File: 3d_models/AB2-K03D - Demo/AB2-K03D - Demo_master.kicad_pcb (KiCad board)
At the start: 2 copper layers, 209 parts

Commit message: AB2-K03D: rename master file
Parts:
- added AB2_STANDOFF_1.96x1.96_BOARD_ROUNDED_CORNERS_KEEPOUT_FR4: VAL**, AB2_STANDOFF_1.96x1.96_BOARD_ROUNDED_CORNERS_KEEPOUT_FR4, F.Cu at (304.8, 166.4)
- added AB2_STANDOFF_1.96x3.92_BOARD_ROUNDED_CORNERS_KEEPOUT_FR4: VAL**, AB2_STANDOFF_1.96x3.92_BOARD_ROUNDED_CORNERS_KEEPOUT_FR4, F.Cu at (356.9, 166.4)
- added AB2_STANDOFF_3.92x3.92_BOARD_ROUNDED_CORNERS_KEEPOUT_FR4: VAL**, AB2_STANDOFF_3.92x3.92_BOARD_ROUNDED_CORNERS_KEEPOUT_FR4, F.Cu at (306.1, 268.0)
- added ROT_ENC1: AB2_ROT_ENC_W_SW, AB2_ROTARY_ENCODER_W_SWITCH, F.Cu at (20.3, 196.8)

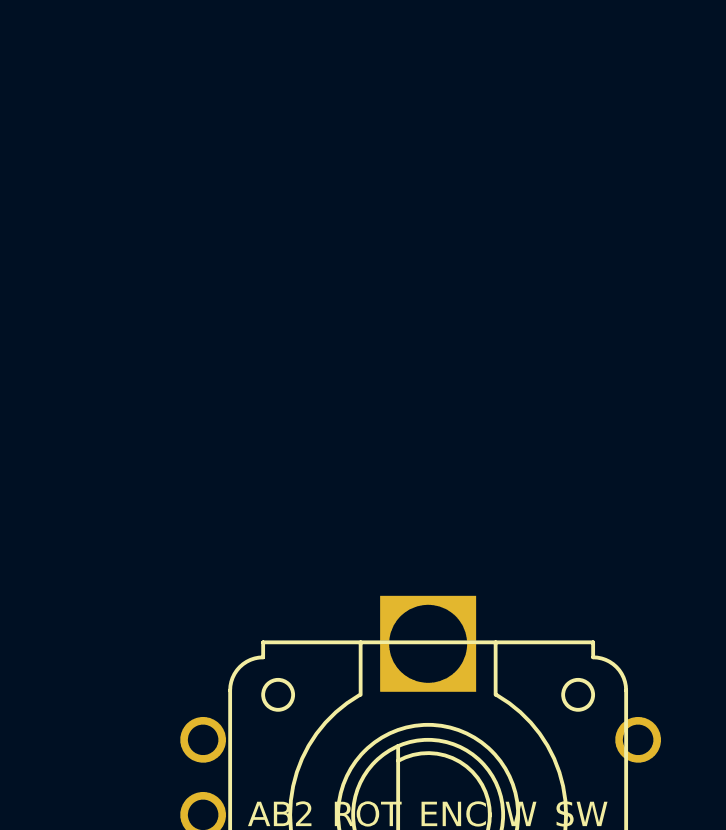
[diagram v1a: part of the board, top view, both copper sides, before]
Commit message: AB2-K03D: add 0805 LED RED/YEL/GRN/BLU
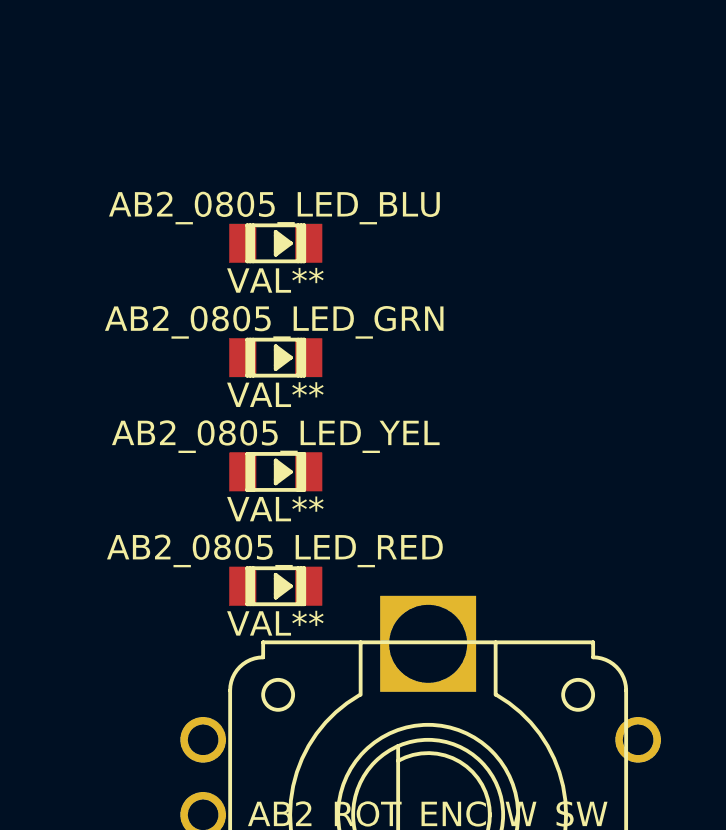
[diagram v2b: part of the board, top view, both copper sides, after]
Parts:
- added AB2_0805_LED_BLU: VAL**, AB2_0805_LED_BLU, F.Cu at (15.2, 177.8)
- added AB2_0805_LED_GRN: VAL**, AB2_0805_LED_GRN, F.Cu at (15.2, 181.6)
- added AB2_0805_LED_RED: VAL**, AB2_0805_LED_RED, F.Cu at (15.2, 189.2)
- added AB2_0805_LED_YEL: VAL**, AB2_0805_LED_YEL, F.Cu at (15.2, 185.4)
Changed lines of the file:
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@@
     (tracks 0)
     (zones 0)
-    (modules 213)
+    (modules 217)
     (nets 9)
   )
@@
     )
   )
+  (module AB2_0805_LED_RED (layer F.Cu)
+    (at 15.24 189.23)
+    (fp_text reference AB2_0805_LED_RED (at 0 -1.27) (layer F.SilkS)
+      (effects (font (size 0.8128 0.8128) (thickness 0.0762)))
+    )
+    (fp_text value VAL** (at 0 1.27) (layer F.SilkS)
+      (effects (font (size 0.8128 0.8128) (thickness 0.0762)))
+    )
+    (fp_line (start 0.254 -0.127) (end 0.254 0.127) (layer F.SilkS) (width 0.127))
+    (fp_line (start 0.381 0) (end 0 0.254) (layer F.SilkS) (width 0.127))
+    (fp_line (start 0.381 0) (end 0 -0.254) (layer F.SilkS) (width 0.127))
+    (fp_line (start 0.127 -0.254) (end 0.127 0.254) (layer F.SilkS) (width 0.127))
+    (fp_line (start 0 -0.381) (end 0 0.381) (layer F.SilkS) (width 0.127))
+    (fp_line (start 0 0.381) (end 0.508 0) (layer F.SilkS) (width 0.127))
+    (fp_line (start 0.508 0) (end 0 -0.381) (layer F.SilkS) (width 0.127))
+    (fp_line (start 0.85 0.6) (end 0.85 -0.6) (layer F.SilkS) (width 0.127))
+    (fp_line (start 0.75 -0.6) (end 0.75 0.6) (layer F.SilkS) (width 0.127))
+    (fp_line (start -0.85 0.6) (end -0.85 -0.6) (layer F.SilkS) (width 0.127))
+    (fp_line (start -0.75 -0.6) (end -0.75 0.6) (layer F.SilkS) (width 0.127))
+    (fp_line (start -0.95 -0.6) (end 0.95 -0.6) (layer F.SilkS) (width 0.127))
+    (fp_line (start 0.95 -0.6) (end 0.95 0.6) (layer F.SilkS) (width 0.127))
+    (fp_line (start 0.95 0.6) (end -0.95 0.6) (layer F.SilkS) (width 0.127))
+    (fp_line (start -0.95 0.6) (end -0.95 -0.6) (layer F.SilkS) (width 0.127))
+    (pad 1 smd rect (at -1.1 0) (size 0.9 1.3)
+      (layers F.Cu F.Paste F.Mask)
+    )
+    (pad 2 smd rect (at 1.1 0) (size 0.9 1.3)
+      (layers F.Cu F.Paste F.Mask)
+    )
+    (model ../3d_models/ab2_passive/AB2_0805_LED_RED.wrl
+      (at (xyz 0 0 0))
+      (scale (xyz 0.3937 0.3937 0.3937))
+      (rotate (xyz 0 0 0))
+    )
+  )
+  (module AB2_0805_LED_YEL (layer F.Cu)
+    (at 15.24 185.42)
+    (fp_text reference AB2_0805_LED_YEL (at 0 -1.27) (layer F.SilkS)
+      (effects (font (size 0.8128 0.8128) (thickness 0.0762)))
+    )
+    (fp_text value VAL** (at 0 1.27) (layer F.SilkS)
+      (effects (font (size 0.8128 0.8128) (thickness 0.0762)))
+    )
+    (fp_line (start 0.254 -0.127) (end 0.254 0.127) (layer F.SilkS) (width 0.127))
+    (fp_line (start 0.381 0) (end 0 0.254) (layer F.SilkS) (width 0.127))
+    (fp_line (start 0.381 0) (end 0 -0.254) (layer F.SilkS) (width 0.127))
+    (fp_line (start 0.127 -0.254) (end 0.127 0.254) (layer F.SilkS) (width 0.127))
+    (fp_line (start 0 -0.381) (end 0 0.381) (layer F.SilkS) (width 0.127))
+    (fp_line (start 0 0.381) (end 0.508 0) (layer F.SilkS) (width 0.127))
+    (fp_line (start 0.508 0) (end 0 -0.381) (layer F.SilkS) (width 0.127))
+    (fp_line (start 0.85 0.6) (end 0.85 -0.6) (layer F.SilkS) (width 0.127))
+    (fp_line (start 0.75 -0.6) (end 0.75 0.6) (layer F.SilkS) (width 0.127))
+    (fp_line (start -0.85 0.6) (end -0.85 -0.6) (layer F.SilkS) (width 0.127))
+    (fp_line (start -0.75 -0.6) (end -0.75 0.6) (layer F.SilkS) (width 0.127))
+    (fp_line (start -0.95 -0.6) (end 0.95 -0.6) (layer F.SilkS) (width 0.127))
+    (fp_line (start 0.95 -0.6) (end 0.95 0.6) (layer F.SilkS) (width 0.127))
+    (fp_line (start 0.95 0.6) (end -0.95 0.6) (layer F.SilkS) (width 0.127))
+    (fp_line (start -0.95 0.6) (end -0.95 -0.6) (layer F.SilkS) (width 0.127))
+    (pad 1 smd rect (at -1.1 0) (size 0.9 1.3)
+      (layers F.Cu F.Paste F.Mask)
+    )
+    (pad 2 smd rect (at 1.1 0) (size 0.9 1.3)
+      (layers F.Cu F.Paste F.Mask)
+    )
+    (model ../3d_models/ab2_passive/AB2_0805_LED_YEL.wrl
+      (at (xyz 0 0 0))
+      (scale (xyz 0.3937 0.3937 0.3937))
+      (rotate (xyz 0 0 0))
+    )
+  )
+  (module AB2_0805_LED_GRN (layer F.Cu)
+    (at 15.24 181.61)
+    (fp_text reference AB2_0805_LED_GRN (at 0 -1.27) (layer F.SilkS)
+      (effects (font (size 0.8128 0.8128) (thickness 0.0762)))
+    )
+    (fp_text value VAL** (at 0 1.27) (layer F.SilkS)
+      (effects (font (size 0.8128 0.8128) (thickness 0.0762)))
+    )
+    (fp_line (start 0.254 -0.127) (end 0.254 0.127) (layer F.SilkS) (width 0.127))
+    (fp_line (start 0.381 0) (end 0 0.254) (layer F.SilkS) (width 0.127))
+    (fp_line (start 0.381 0) (end 0 -0.254) (layer F.SilkS) (width 0.127))
+    (fp_line (start 0.127 -0.254) (end 0.127 0.254) (layer F.SilkS) (width 0.127))
+    (fp_line (start 0 -0.381) (end 0 0.381) (layer F.SilkS) (width 0.127))
+    (fp_line (start 0 0.381) (end 0.508 0) (layer F.SilkS) (width 0.127))
+    (fp_line (start 0.508 0) (end 0 -0.381) (layer F.SilkS) (width 0.127))
+    (fp_line (start 0.85 0.6) (end 0.85 -0.6) (layer F.SilkS) (width 0.127))
+    (fp_line (start 0.75 -0.6) (end 0.75 0.6) (layer F.SilkS) (width 0.127))
+    (fp_line (start -0.85 0.6) (end -0.85 -0.6) (layer F.SilkS) (width 0.127))
+    (fp_line (start -0.75 -0.6) (end -0.75 0.6) (layer F.SilkS) (width 0.127))
+    (fp_line (start -0.95 -0.6) (end 0.95 -0.6) (layer F.SilkS) (width 0.127))
+    (fp_line (start 0.95 -0.6) (end 0.95 0.6) (layer F.SilkS) (width 0.127))
+    (fp_line (start 0.95 0.6) (end -0.95 0.6) (layer F.SilkS) (width 0.127))
+    (fp_line (start -0.95 0.6) (end -0.95 -0.6) (layer F.SilkS) (width 0.127))
+    (pad 1 smd rect (at -1.1 0) (size 0.9 1.3)
+      (layers F.Cu F.Paste F.Mask)
+    )
+    (pad 2 smd rect (at 1.1 0) (size 0.9 1.3)
+      (layers F.Cu F.Paste F.Mask)
+    )
+    (model ../3d_models/ab2_passive/AB2_0805_LED_GRN.wrl
+      (at (xyz 0 0 0))
+      (scale (xyz 0.3937 0.3937 0.3937))
+      (rotate (xyz 0 0 0))
+    )
+  )
+  (module AB2_0805_LED_BLU (layer F.Cu)
+    (at 15.24 177.8)
+    (fp_text reference AB2_0805_LED_BLU (at 0 -1.27) (layer F.SilkS)
+      (effects (font (size 0.8128 0.8128) (thickness 0.0762)))
+    )
+    (fp_text value VAL** (at 0 1.27) (layer F.SilkS)
+      (effects (font (size 0.8128 0.8128) (thickness 0.0762)))
+    )
+    (fp_line (start 0.254 -0.127) (end 0.254 0.127) (layer F.SilkS) (width 0.127))
+    (fp_line (start 0.381 0) (end 0 0.254) (layer F.SilkS) (width 0.127))
+    (fp_line (start 0.381 0) (end 0 -0.254) (layer F.SilkS) (width 0.127))
+    (fp_line (start 0.127 -0.254) (end 0.127 0.254) (layer F.SilkS) (width 0.127))
+    (fp_line (start 0 -0.381) (end 0 0.381) (layer F.SilkS) (width 0.127))
+    (fp_line (start 0 0.381) (end 0.508 0) (layer F.SilkS) (width 0.127))
+    (fp_line (start 0.508 0) (end 0 -0.381) (layer F.SilkS) (width 0.127))
+    (fp_line (start 0.85 0.6) (end 0.85 -0.6) (layer F.SilkS) (width 0.127))
+    (fp_line (start 0.75 -0.6) (end 0.75 0.6) (layer F.SilkS) (width 0.127))
+    (fp_line (start -0.85 0.6) (end -0.85 -0.6) (layer F.SilkS) (width 0.127))
+    (fp_line (start -0.75 -0.6) (end -0.75 0.6) (layer F.SilkS) (width 0.127))
+    (fp_line (start -0.95 -0.6) (end 0.95 -0.6) (layer F.SilkS) (width 0.127))
+    (fp_line (start 0.95 -0.6) (end 0.95 0.6) (layer F.SilkS) (width 0.127))
+    (fp_line (start 0.95 0.6) (end -0.95 0.6) (layer F.SilkS) (width 0.127))
+    (fp_line (start -0.95 0.6) (end -0.95 -0.6) (layer F.SilkS) (width 0.127))
+    (pad 1 smd rect (at -1.1 0) (size 0.9 1.3)
+      (layers F.Cu F.Paste F.Mask)
+    )
+    (pad 2 smd rect (at 1.1 0) (size 0.9 1.3)
+      (layers F.Cu F.Paste F.Mask)
+    )
+    (model ../3d_models/ab2_passive/AB2_0805_LED_BLU.wrl
+      (at (xyz 0 0 0))
+      (scale (xyz 0.3937 0.3937 0.3937))
+      (rotate (xyz 0 0 0))
+    )
+  )

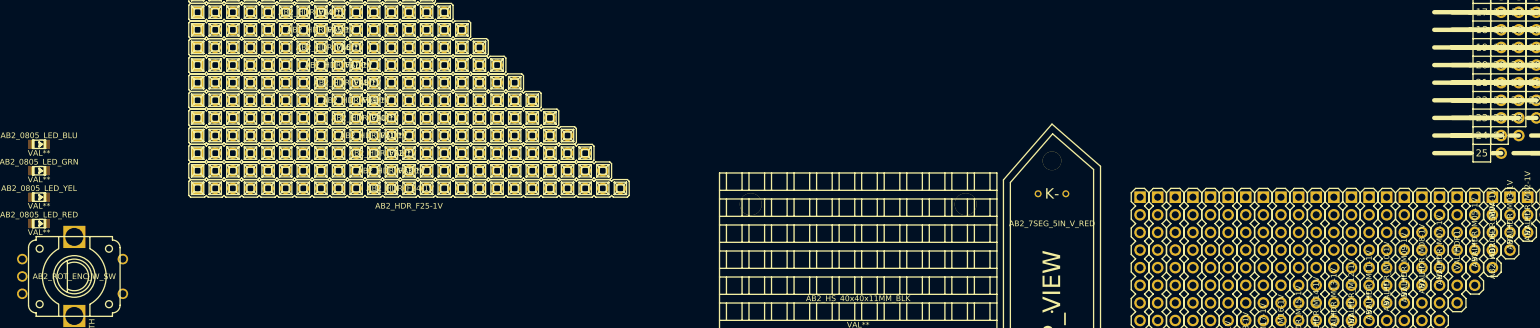
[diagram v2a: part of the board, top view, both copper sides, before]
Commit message: AB2-K03D: add 5050 RGB LEDs to master
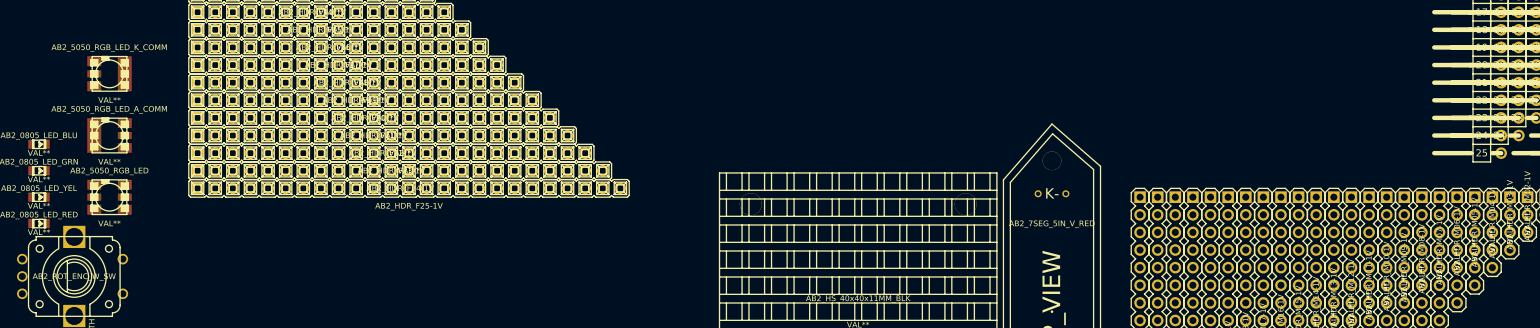
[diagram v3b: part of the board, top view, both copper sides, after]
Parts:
- removed HDR1: AB2_HDR06-1_SBW, AB2_HDR_M06-1V
- added AB2_5050_RGB_LED: VAL**, AB2_5050_RGB_LED, F.Cu at (25.4, 185.4)
- added AB2_5050_RGB_LED_A_COMM: VAL**, AB2_5050_RGB_LED_A_COMM, F.Cu at (25.4, 176.5)
- added AB2_5050_RGB_LED_K_COMM: VAL**, AB2_5050_RGB_LED_K_COMM, F.Cu at (25.4, 167.6)
- added AB2_HDR_M06-1V: VAL**, AB2_HDR_M06-1V, F.Cu at (222.2, 191.8)
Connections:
- ROT_ENC1 pad 1: /R_ENCA -> (no net)
- ROT_ENC1 pad 2: GND -> (no net)
- ROT_ENC1 pad 3: /R_ENCB -> (no net)
- ROT_ENC1 pad 4: /R_SW+ -> (no net)
- ROT_ENC1 pad 6: GND -> (no net)

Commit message: 3d_models: AB2-K03D: add 2x3 idc to master
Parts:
- added AB2_HDR_M03-2V-S: VAL**, AB2_HDR_M03-2V-S, F.Cu at (207.0, 179.1)
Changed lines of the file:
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@@
     (tracks 0)
     (zones 0)
-    (modules 220)
+    (modules 221)
     (nets 1)
   )
@@
       (at (xyz 0 0 0))
       (scale (xyz 0.3937 0.3937 0.3937))
+      (rotate (xyz 0 0 0))
+    )
+  )
+  (module AB2_HDR_M03-2V-S (layer F.Cu)
+    (at 207.01 179.07)
+    (fp_text reference AB2_HDR_M03-2V-S (at 0 5.08) (layer F.SilkS)
+      (effects (font (size 0.8128 0.8128) (thickness 0.0762)))
+    )
+    (fp_text value VAL** (at 0 -5.08) (layer F.SilkS)
+      (effects (font (size 0.8128 0.8128) (thickness 0.0762)))
+    )
+    (fp_line (start 2.032 3.302) (end 2.032 4.191) (layer F.SilkS) (width 0.127))
+    (fp_line (start -2.032 3.302) (end -2.032 4.191) (layer F.SilkS) (width 0.127))
+    (fp_line (start -2.794 2.794) (end -2.286 2.794) (layer F.SilkS) (width 0.127))
+    (fp_line (start -2.413 2.794) (end -2.54 2.921) (layer F.SilkS) (width 0.127))
+    (fp_line (start -2.667 2.794) (end -2.54 2.921) (layer F.SilkS) (width 0.127))
+    (fp_line (start -2.286 2.794) (end -2.54 3.048) (layer F.SilkS) (width 0.127))
+    (fp_line (start -2.794 2.794) (end -2.54 3.048) (layer F.SilkS) (width 0.127))
+    (fp_line (start 6.477 -3.302) (end -6.477 -3.302) (layer F.SilkS) (width 0.127))
+    (fp_line (start -6.477 -3.302) (end -6.477 3.302) (layer F.SilkS) (width 0.127))
+    (fp_line (start -6.477 3.302) (end 6.477 3.302) (layer F.SilkS) (width 0.127))
+    (fp_line (start 6.477 3.302) (end 6.477 -3.302) (layer F.SilkS) (width 0.127))
+    (fp_line (start 7.62 -4.191) (end -7.62 -4.191) (layer F.SilkS) (width 0.127))
+    (fp_line (start -7.62 -4.191) (end -7.62 4.191) (layer F.SilkS) (width 0.127))
+    (fp_line (start -7.62 4.191) (end 7.62 4.191) (layer F.SilkS) (width 0.127))
+    (fp_line (start 7.62 4.191) (end 7.62 -4.191) (layer F.SilkS) (width 0.127))
+    (fp_line (start -2.794 2.54) (end -2.286 2.54) (layer F.SilkS) (width 0.127))
+    (fp_line (start 1.27 -1.905) (end 1.905 -2.54) (layer F.SilkS) (width 0.127))
+    (fp_line (start 1.905 -2.54) (end 3.175 -2.54) (layer F.SilkS) (width 0.127))
+    (fp_line (start 3.175 -2.54) (end 3.81 -1.905) (layer F.SilkS) (width 0.127))
+    (fp_line (start 3.81 -1.905) (end 3.81 1.905) (layer F.SilkS) (width 0.127))
+    (fp_line (start 3.81 1.905) (end 3.175 2.54) (layer F.SilkS) (width 0.127))
+    (fp_line (start 3.175 2.54) (end 1.905 2.54) (layer F.SilkS) (width 0.127))
+    (fp_line (start 1.905 2.54) (end 1.27 1.905) (layer F.SilkS) (width 0.127))
+    (fp_line (start -1.27 -1.905) (end -0.635 -2.54) (layer F.SilkS) (width 0.127))
+    (fp_line (start -0.635 -2.54) (end 0.635 -2.54) (layer F.SilkS) (width 0.127))
+    (fp_line (start 0.635 -2.54) (end 1.27 -1.905) (layer F.SilkS) (width 0.127))
+    (fp_line (start 1.27 -1.905) (end 1.27 1.905) (layer F.SilkS) (width 0.127))
+    (fp_line (start 1.27 1.905) (end 0.635 2.54) (layer F.SilkS) (width 0.127))
+    (fp_line (start 0.635 2.54) (end -0.635 2.54) (layer F.SilkS) (width 0.127))
+    (fp_line (start -0.635 2.54) (end -1.27 1.905) (layer F.SilkS) (width 0.127))
+    (fp_line (start -3.175 2.54) (end -3.81 1.905) (layer F.SilkS) (width 0.127))
+    (fp_line (start -3.81 1.905) (end -3.81 -1.905) (layer F.SilkS) (width 0.127))
+    (fp_line (start -3.81 -1.905) (end -3.175 -2.54) (layer F.SilkS) (width 0.127))
+    (fp_line (start -3.175 -2.54) (end -1.905 -2.54) (layer F.SilkS) (width 0.127))
+    (fp_line (start -1.905 -2.54) (end -1.27 -1.905) (layer F.SilkS) (width 0.127))
+    (fp_line (start -1.27 -1.905) (end -1.27 1.905) (layer F.SilkS) (width 0.127))
+    (fp_line (start -1.27 1.905) (end -1.905 2.54) (layer F.SilkS) (width 0.127))
+    (fp_line (start -1.905 2.54) (end -3.175 2.54) (layer F.SilkS) (width 0.127))
+    (pad 1 thru_hole circle (at -2.54 1.27) (size 1.6764 1.6764) (drill 1.016)
+      (layers *.Cu *.Mask F.SilkS)
+    )
+    (pad 2 thru_hole circle (at -2.54 -1.27) (size 1.6764 1.6764) (drill 1.016)
+      (layers *.Cu *.Mask F.SilkS)
+    )
+    (pad 3 thru_hole circle (at 0 1.27) (size 1.6764 1.6764) (drill 1.016)
+      (layers *.Cu *.Mask F.SilkS)
+    )
+    (pad 4 thru_hole circle (at 0 -1.27) (size 1.6764 1.6764) (drill 1.016)
+      (layers *.Cu *.Mask F.SilkS)
+    )
+    (pad 5 thru_hole circle (at 2.54 1.27) (size 1.6764 1.6764) (drill 1.016)
+      (layers *.Cu *.Mask F.SilkS)
+    )
+    (pad 6 thru_hole circle (at 2.54 -1.27) (size 1.6764 1.6764) (drill 1.016)
+      (layers *.Cu *.Mask F.SilkS)
+    )
+    (model ../3d_models/ab2_idc/AB2_HDR_M03-2V-S-3M.wrl
+      (at (xyz 0 0 0))
+      (scale (xyz 0.3937 0.3937 0.3937))

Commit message: 3d_models: AB2-K03D: add 2x4 pin box shrouded header
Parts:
- added AB2_HDR_M04-2V-S: VAL**, AB2_HDR_M04-2V-S, F.Cu at (205.7, 170.2)
- AB2_TSSOP30_W: renamed from AB2_TSSOP30; footprint AB2_TSSOP30 -> AB2_TSSOP30_W
- AB2_TSSOP32_W: renamed from AB2_TSSOP32; footprint AB2_TSSOP32 -> AB2_TSSOP32_W
- AB2_TSSOP38: footprint AB2_TSSOP38 -> AB2_TSSOP38_W
